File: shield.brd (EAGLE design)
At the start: 25.6 x 28 mm, 13 parts

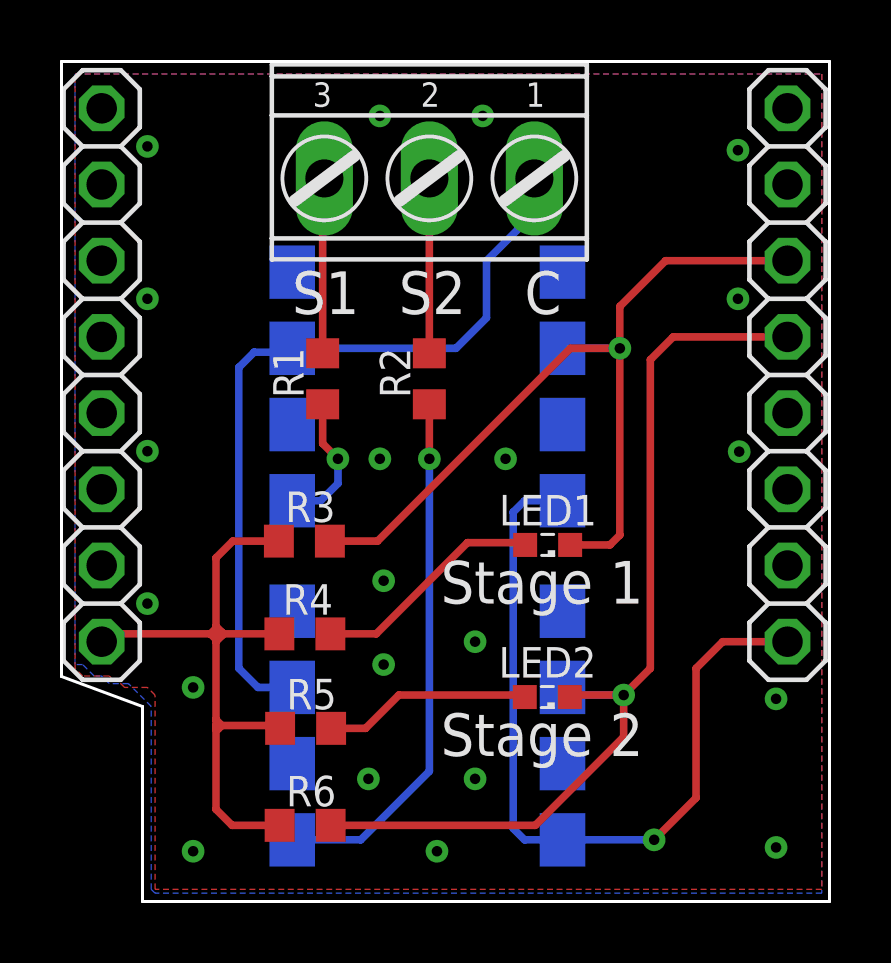
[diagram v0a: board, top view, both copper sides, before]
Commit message: board tweaks, bom fix, local library added
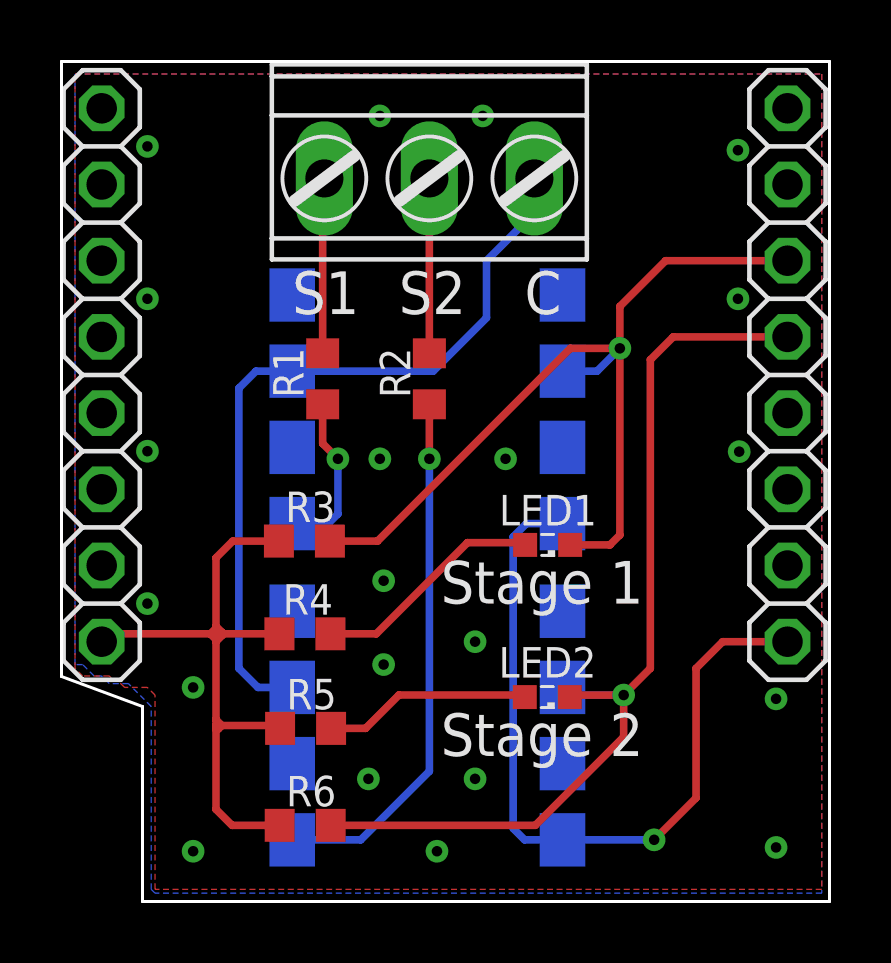
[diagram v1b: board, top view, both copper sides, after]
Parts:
- U$1, U$2: device ICCollection:SMT8 -> shield:SMT8
- X1: device con-ptr500:AK550/3 -> shield:AK550/3-N
- moved U$1 0.76 mm to (7.81, 12.7)
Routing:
- net N$10: track 4.61 -> 5.71 mm
- net 5V: track 26.9 -> 26.1 mm
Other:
- board text added: "Compressor Status v1.1"
- board text removed: "."
- board text removed: "Compressor Status v1.0"
